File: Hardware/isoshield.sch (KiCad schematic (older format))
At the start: 2 parts, among them J3 CAN_TRA_HEADER, J4 CAN_IMP_HEADER

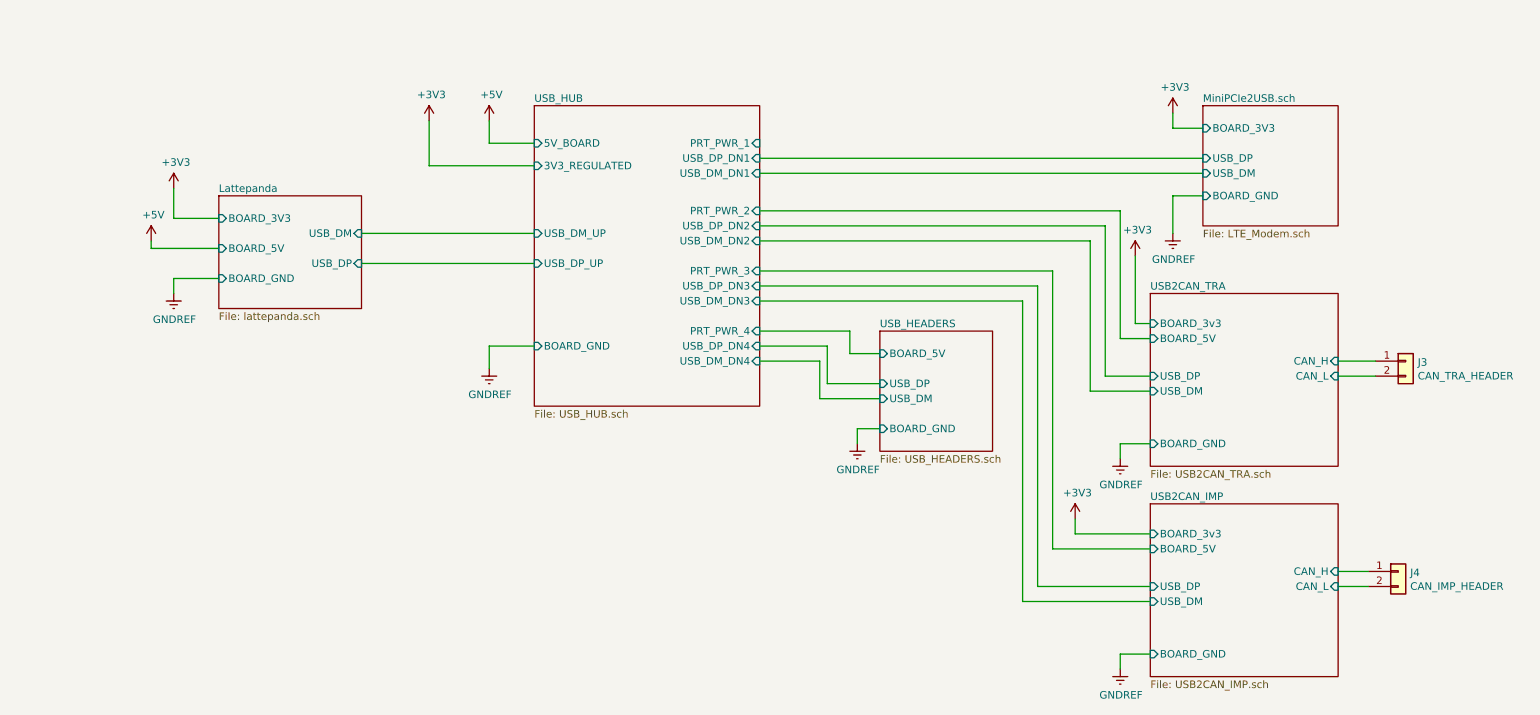
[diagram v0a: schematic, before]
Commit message: Added footprints to schematic symbols
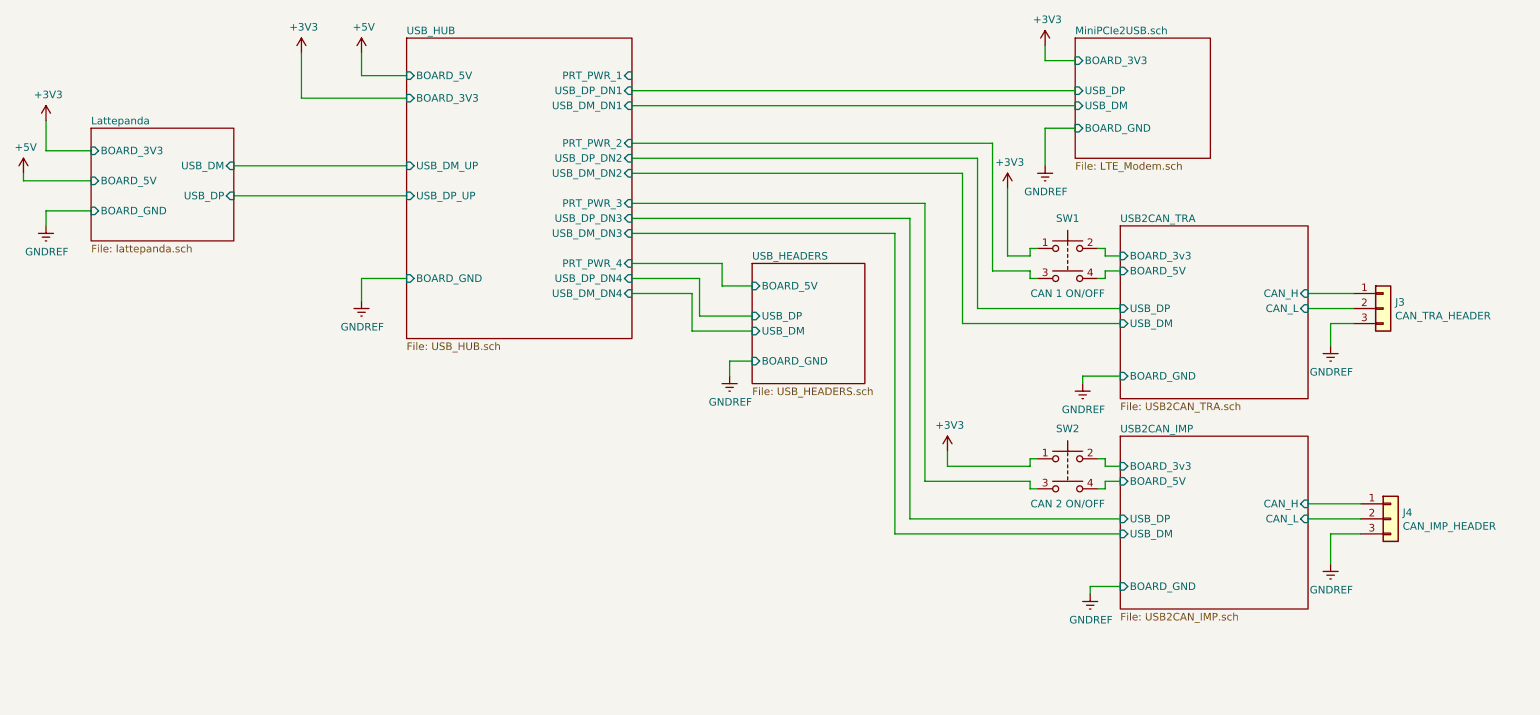
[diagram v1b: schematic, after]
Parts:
- removed J3: CAN_TRA_HEADER, TerminalBlock_Phoenix:TerminalBlock_Phoenix_PT-1,5-2-5.0-H_1x02_P5.00mm_Horizontal, symbol Connector_Generic:Conn_01x02
- removed J4: CAN_IMP_HEADER, TerminalBlock_Phoenix:TerminalBlock_Phoenix_PT-1,5-2-5.0-H_1x02_P5.00mm_Horizontal, symbol Connector_Generic:Conn_01x02
- added J3: CAN_TRA_HEADER, TerminalBlock_Phoenix:TerminalBlock_Phoenix_MKDS-1,5-3-5.08_1x03_P5.08mm_Horizontal, symbol Connector_Generic:Conn_01x03
- added J4: CAN_IMP_HEADER, TerminalBlock_Phoenix:TerminalBlock_Phoenix_MKDS-1,5-3-5.08_1x03_P5.08mm_Horizontal, symbol Connector_Generic:Conn_01x03
- added SW1: CAN 1 ON/OFF, Button_Switch_SMD:SW_MEC_5GSH9, symbol Switch:SW_Push_Dual
- added SW2: CAN 2 ON/OFF, Button_Switch_SMD:SW_MEC_5GSH9, symbol Switch:SW_Push_Dual
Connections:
- net +3V3: now also SW1.1, SW2.1
- net GNDREF: now also J3.3 (Pin_3), J4.3 (Pin_3)
- net USB2CAN_IMP/BOARD_5V: now also SW2.4
- net USB2CAN_IMP/CAN_H: now also J4.1 (Pin_1)
- net USB2CAN_IMP/CAN_L: now also J4.2 (Pin_2)
- net USB2CAN_TRA/BOARD_5V: now also SW1.4
- net USB2CAN_TRA/CAN_H: now also J3.1 (Pin_1)
- net USB2CAN_TRA/CAN_L: now also J3.2 (Pin_2)
- new net USB2CAN_IMP/BOARD_3v3: SW2.2
- new net USB2CAN_TRA/BOARD_3v3: SW1.2
- new net USB_HUB/PRT_PWR_2: SW1.3
- new net USB_HUB/PRT_PWR_3: SW2.3
